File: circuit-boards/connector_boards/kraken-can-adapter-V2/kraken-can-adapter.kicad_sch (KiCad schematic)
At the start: 8 parts, among them J1 CAN, J2 CAN, J3 CAN_L, J4 CAN_H

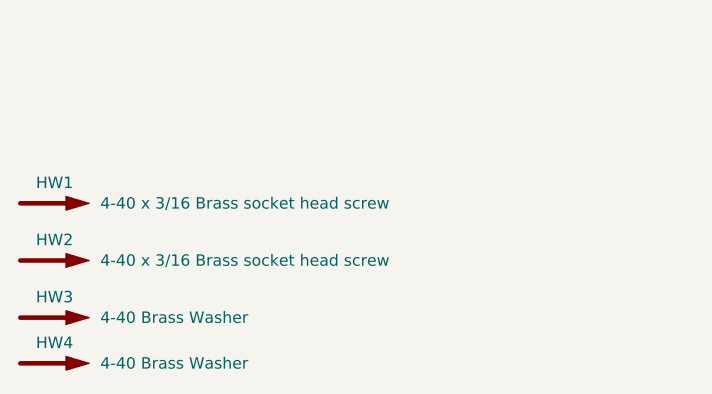
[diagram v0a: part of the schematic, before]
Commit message: Fixed kraken-can-adapter V2.
Signed-off-by: Scott Berman <scott.berman@bluerivertech.com>
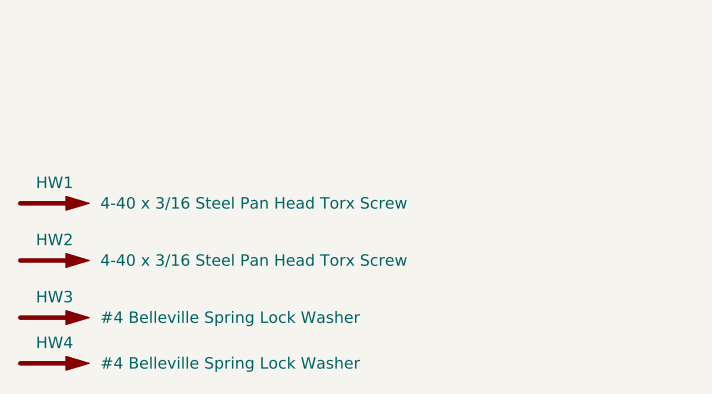
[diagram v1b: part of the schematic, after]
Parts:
- HW1, HW2: value 4-40 x 3/16 Brass socket head screw -> 4-40 x 3/16 Steel Pan Head Torx Screw; MFG P/N 93465A103 -> 93701A250
- HW3, HW4: value 4-40 Brass Washer -> #4 Belleville Spring Lock Washer; MFG P/N 92916A320 -> 90895A121
- J1, J2: DIST P/N WM4800-ND -> WM4142-ND; MFG P/N 70543-0001 -> 0705450036
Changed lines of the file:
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@@
 	(title_block
 		(title "Kraken CAN Adapter")
-		(date "2023-12-28")
-		(rev "1")
+		(date "2024-06-22")
+		(rev "2")
 		(company "971 Spartan Robotics")
 	)
@@
 			)
 		)
-		(property "Value" "4-40 x 3/16 Brass socket head screw"
+		(property "Value" "4-40 x 3/16 Steel Pan Head Torx Screw"
 			(at 60.96 152.4 0)
 			(effects
@@
 			)
 		)
-		(property "Datasheet" "https://www.mcmaster.com/93465A103/"
+		(property "Datasheet" "https://www.mcmaster.com/93701A250/"
 			(at 55.88 152.4 0)
 			(effects
@@
 			)
 		)
-		(property "MFG P/N" "93465A103"
+		(property "MFG P/N" "93701A250"
 			(at 55.88 152.4 0)
 			(effects
@@
 			)
 		)
-		(property "Value" "4-40 Brass Washer"
+		(property "Value" "#4 Belleville Spring Lock Washer"
 			(at 60.96 158.75 0)
 			(effects
@@
 			)
 		)
-		(property "Datasheet" "https://www.mcmaster.com/92916A320/"
+		(property "Datasheet" "https://www.mcmaster.com/90895A121/"
 			(at 55.88 158.75 0)
 			(effects
@@
 			)
 		)
-		(property "MFG P/N" "92916A320"
+		(property "MFG P/N" "90895A121"
 			(at 55.88 158.75 0)
 			(effects
@@
 				(path "/a8891e91-a521-46c1-a433-4a59f557fea2"
 					(reference "HW3")
+					(unit 1)
+				)
+			)
+		)
+	)
+	(symbol
+		(lib_id "Graphic:SYM_Arrow_Large")
+		(at 55.88 163.83 0)
+		(unit 1)
+		(exclude_from_sim no)
+		(in_bom yes)
+		(on_board no)
+		(dnp no)
+		(property "Reference" "HW4"
+			(at 55.88 161.544 0)
+			(effects
+				(font
+					(size 1.27 1.27)
+				)
+			)
+		)
+		(property "Value" "#4 Belleville Spring Lock Washer"
+			(at 60.96 163.83 0)
+			(effects
+				(font
+					(size 1.27 1.27)
+				)
+				(justify left)
+			)
+		)
+		(property "Footprint" ""
+			(at 55.88 163.83 0)
+			(effects
+				(font
+					(size 1.27 1.27)
+				)
+				(hide yes)
+			)
+		)
+		(property "Datasheet" "https://www.mcmaster.com/90895A121/"
+			(at 55.88 163.83 0)
+			(effects
+				(font
+					(size 1.27 1.27)
+				)
+				(hide yes)
+			)
+		)
+		(property "Description" ""
+			(at 55.88 163.83 0)
+			(effects
+				(font
+					(size 1.27 1.27)
+				)
+				(hide yes)
+			)
+		)
+		(property "MFG" "McMaster-Carr"
+			(at 55.88 163.83 0)
+			(effects
+				(font
+					(size 1.27 1.27)
+				)
+				(hide yes)
+			)
+		)
+		(property "MFG P/N" "90895A121"
+			(at 55.88 163.83 0)
+			(effects
+				(font
+					(size 1.27 1.27)
+				)
+				(hide yes)
+			)
+		)
+		(instances
+			(project "kraken-can-adapter"
+				(path "/a8891e91-a521-46c1-a433-4a59f557fea2"
+					(reference "HW4")
 					(unit 1)
 				)
@@
 			)
 		)
-		(property "Value" "4-40 x 3/16 Brass socket head screw"
+		(property "Value" "4-40 x 3/16 Steel Pan Head Torx Screw"
 			(at 60.96 146.05 0)
 			(effects
@@
 			)
 		)
-		(property "Datasheet" "https://www.mcmaster.com/93465A103/"
+		(property "Datasheet" "https://www.mcmaster.com/93701A250/"
 			(at 55.88 146.05 0)
 			(effects
@@
 			)
 		)
-		(property "MFG P/N" "93465A103"
+		(property "MFG P/N" "93701A250"
 			(at 55.88 146.05 0)
 			(effects
@@
 			)
 		)
-		(property "MFG P/N" "70543-0001"
+		(property "MFG P/N" "0705450036"
 			(at 156.21 118.11 0)
 			(effects
@@
 			)
 		)
-		(property "DIST P/N" "WM4800-ND"
+		(property "DIST P/N" "WM4142-ND"
 			(at 156.21 118.11 0)
 			(effects
@@
 			)
 		)
-		(property "Datasheet" "~"
+		(property "Datasheet" "Components/Molex-705450011_sd.pdf"
 			(at 156.21 101.6 0)
 			(effects
@@
 			)
 		)
-		(property "MFG P/N" "70543-0001"
+		(property "MFG P/N" "0705450036"
 			(at 156.21 101.6 0)
 			(effects
@@
 			)
 		)
-		(property "DIST P/N" "WM4800-ND"
+		(property "DIST P/N" "WM4142-ND"
 			(at 156.21 101.6 0)
 			(effects
@@
 					(unit 1)
 				)
-			)
-		)
-	)
-	(symbol
-		(lib_id "Graphic:SYM_Arrow_Large")
-		(at 55.88 163.83 0)
-		(unit 1)
-		(exclude_from_sim no)
-		(in_bom yes)
-		(on_board no)
-		(dnp no)
-		(property "Reference" "HW4"
-			(at 55.88 161.544 0)
-			(effects
-				(font
-					(size 1.27 1.27)
-				)
-			)
-		)
-		(property "Value" "4-40 Brass Washer"
-			(at 60.96 163.83 0)
-			(effects
-				(font
-					(size 1.27 1.27)
-				)
-				(justify left)
-			)
-		)
-		(property "Footprint" ""
-			(at 55.88 163.83 0)
-			(effects
-				(font
-					(size 1.27 1.27)
-				)
-				(hide yes)
-			)
-		)
-		(property "Datasheet" "https://www.mcmaster.com/92916A320/"
-			(at 55.88 163.83 0)
-			(effects
-				(font
-					(size 1.27 1.27)
-				)
-				(hide yes)
-			)
-		)
-		(property "Description" ""
-			(at 55.88 163.83 0)
-			(effects
-				(font
-					(size 1.27 1.27)
-				)
-				(hide yes)
-			)
-		)
-		(property "MFG" "McMaster-Carr"
-			(at 55.88 163.83 0)
-			(effects
-				(font
-					(size 1.27 1.27)
-				)
-				(hide yes)
-			)
-		)
-		(property "MFG P/N" "92916A320"
-			(at 55.88 163.83 0)
-			(effects
-				(font
-					(size 1.27 1.27)
-				)
-				(hide yes)
-			)
-		)
-		(instances
-			(project "kraken-can-adapter"
-				(path "/a8891e91-a521-46c1-a433-4a59f557fea2"
-					(reference "HW4")
-					(unit 1)
-				)
